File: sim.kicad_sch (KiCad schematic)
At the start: 40 parts

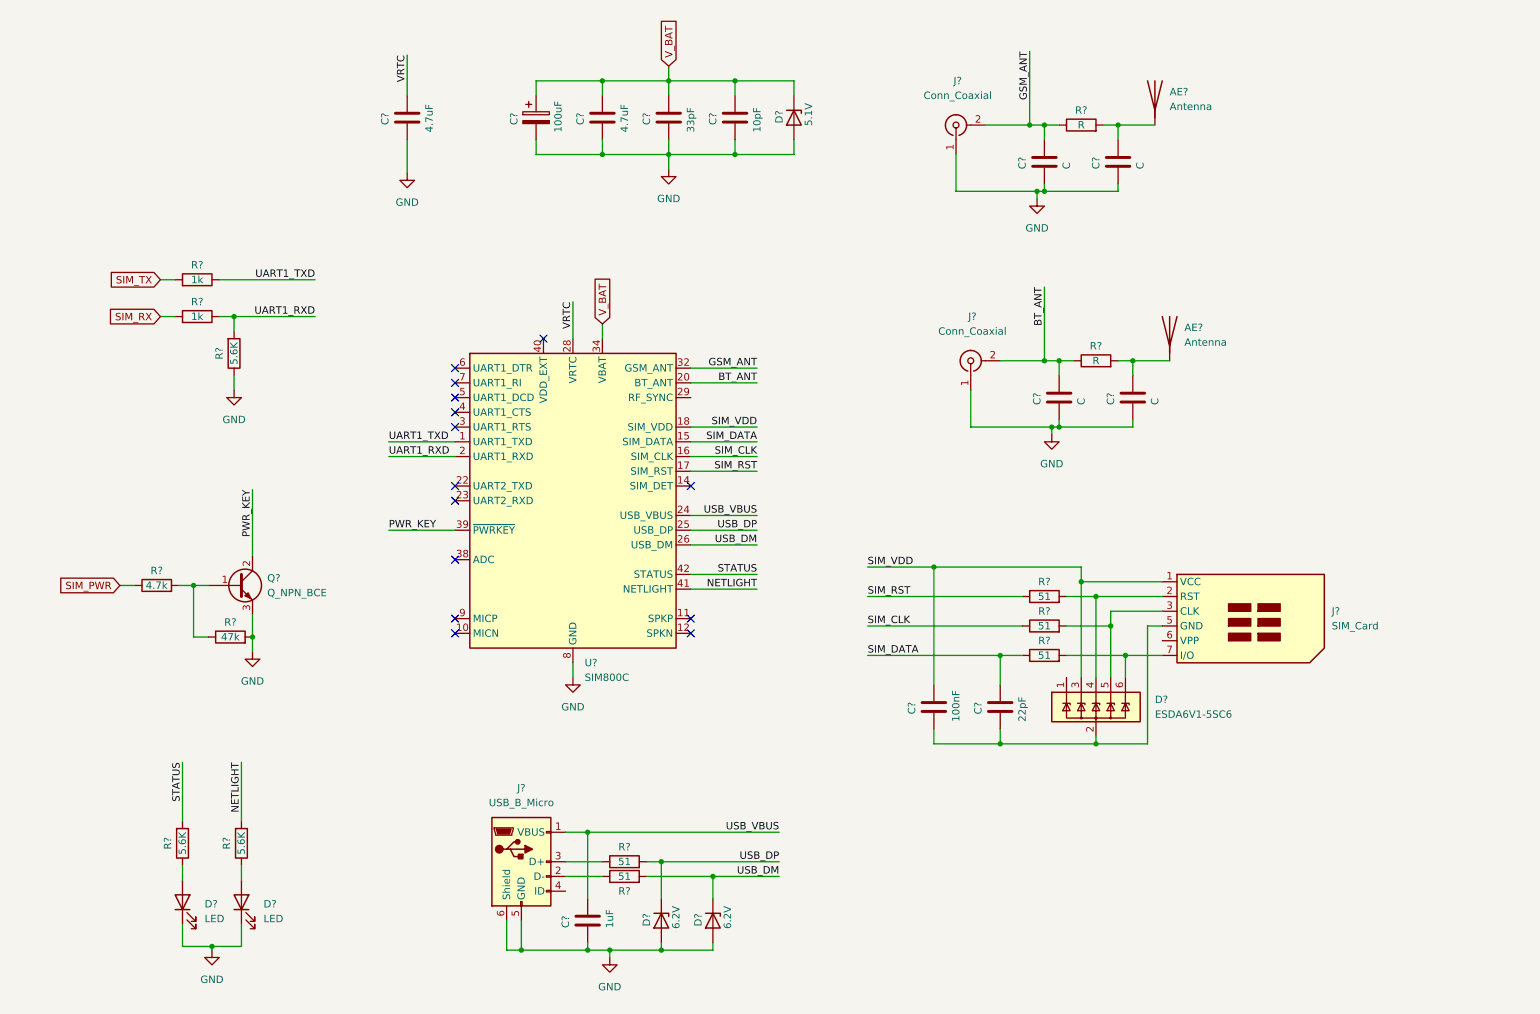
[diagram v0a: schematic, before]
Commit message: Create scheme for MCU with peripheries
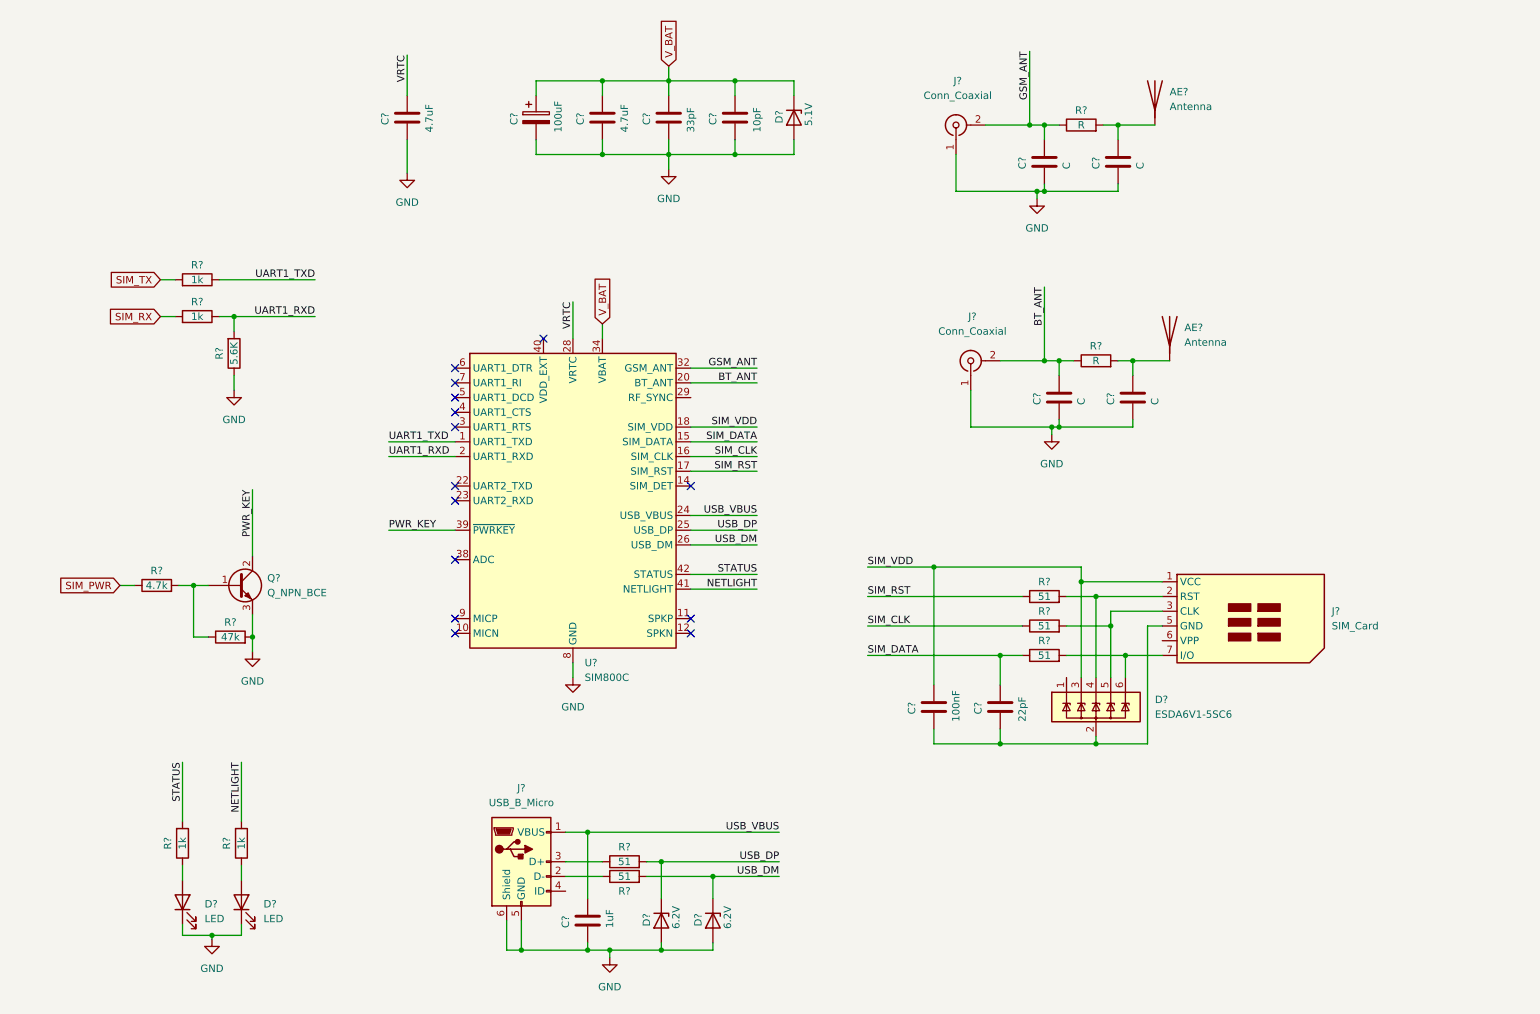
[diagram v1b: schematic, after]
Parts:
- R? (x2): value 5.6K -> 1k
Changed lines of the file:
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@@
   (junction (at 134.62 180.34) (diameter 0) (color 0 0 0 0)
   )
-  (junction (at 57.15 179.705) (diameter 0) (color 0 0 0 0)
+  (junction (at 57.15 177.8) (diameter 0) (color 0 0 0 0)
   )
   (junction (at 212.09 124.46) (diameter 0) (color 0 0 0 0)
@@
     (stroke (width 0) (type default) (color 0 0 0 0))
   )
-  (wire (pts (xy 57.15 179.705) (xy 52.07 179.705))
+  (wire (pts (xy 57.15 177.8) (xy 52.07 177.8))
     (stroke (width 0) (type default) (color 0 0 0 0))
   )
@@
     (stroke (width 0) (type default) (color 0 0 0 0))
   )
-  (wire (pts (xy 57.15 179.705) (xy 62.23 179.705))
+  (wire (pts (xy 57.15 177.8) (xy 62.23 177.8))
     (stroke (width 0) (type default) (color 0 0 0 0))
   )
@@
     (stroke (width 0) (type default) (color 0 0 0 0))
   )
-  (wire (pts (xy 52.07 175.895) (xy 52.07 179.705))
+  (wire (pts (xy 52.07 175.895) (xy 52.07 177.8))
     (stroke (width 0) (type default) (color 0 0 0 0))
   )
@@
     (stroke (width 0) (type default) (color 0 0 0 0))
   )
-  (wire (pts (xy 62.23 175.895) (xy 62.23 179.705))
+  (wire (pts (xy 62.23 175.895) (xy 62.23 177.8))
     (stroke (width 0) (type default) (color 0 0 0 0))
   )
@@
     (stroke (width 0) (type default) (color 0 0 0 0))
   )
-  (wire (pts (xy 57.15 180.34) (xy 57.15 179.705))
+  (wire (pts (xy 57.15 178.435) (xy 57.15 177.8))
     (stroke (width 0) (type default) (color 0 0 0 0))
   )
@@
     (in_bom yes) (on_board yes)
     (property "Reference" "R?" (id 0) (at 59.69 161.925 90))
-    (property "Value" "5.6K" (id 1) (at 62.23 161.925 90))
+    (property "Value" "1k" (id 1) (at 62.23 161.925 90))
     (property "Footprint" "" (id 2) (at 60.452 161.925 90)
       (effects (font (size 1.27 1.27)) hide)
@@
     (in_bom yes) (on_board yes)
     (property "Reference" "R?" (id 0) (at 49.53 161.925 90))
-    (property "Value" "5.6K" (id 1) (at 52.07 161.925 90))
+    (property "Value" "1k" (id 1) (at 52.07 161.925 90))
     (property "Footprint" "" (id 2) (at 50.292 161.925 90)
       (effects (font (size 1.27 1.27)) hide)
@@
     (pin "1")
   )
-  (symbol (lib_id "power:GND") (at 57.15 180.34 0) (unit 1)
-    (in_bom yes) (on_board yes) (fields_autoplaced)
-    (property "Reference" "#PWR?" (id 0) (at 57.15 186.69 0)
-      (effects (font (size 1.27 1.27)) hide)
-    )
-    (property "Value" "GND" (id 1) (at 57.15 185.42 0))
-    (property "Footprint" "" (id 2) (at 57.15 180.34 0)
-      (effects (font (size 1.27 1.27)) hide)
-    )
-    (property "Datasheet" "" (id 3) (at 57.15 180.34 0)
-      (effects (font (size 1.27 1.27)) hide)
-    )
+  (symbol (lib_id "power:GND") (at 57.15 178.435 0) (unit 1)
+    (in_bom yes) (on_board yes) (fields_autoplaced)
+    (property "Reference" "#PWR?" (id 0) (at 57.15 184.785 0)
+      (effects (font (size 1.27 1.27)) hide)
+    )
+    (property "Value" "GND" (id 1) (at 57.15 183.515 0))
+    (property "Footprint" "" (id 2) (at 57.15 178.435 0)
+      (effects (font (size 1.27 1.27)) hide)
+    )
+    (property "Datasheet" "" (id 3) (at 57.15 178.435 0)
+      (effects (font (size 1.27 1.27)) hide)
+    )

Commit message: Change layout
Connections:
- net NETLIGHT: no longer names the net of R?.2
- net NETLIGHT: now also U?.42 (STATUS); no longer U?.41 (NETLIGHT)
- net STATUS: no longer names the net of R?.2
- net STATUS: now also U?.41 (NETLIGHT); no longer U?.42 (STATUS)
- net UART1_RXD: no longer names the net of R?.1, R?.2, U?.2 (UART1_RXD)
- net UART1_TXD: no longer names the net of R?.1, U?.1 (UART1_TXD)
- net VRTC: no longer names the net of C?.1, U?.28 (VRTC)
- no-connect marks 14 -> 15
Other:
- moved on the sheet: AE?, C?, D?, J?, Q?, R?

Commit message: Add TSP62851x library and LDO on PSU scheme
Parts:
- removed AE? (x2): Antenna, symbol Device:Antenna
- removed C? (x4): C, symbol Device:C
- removed J?: Conn_Coaxial, symbol Connector:Conn_Coaxial
- removed R? (x2): R, symbol Device:R
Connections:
- net BT_ANT: no longer names the net of U?.20 (BT_ANT)
- net V_BAT renamed +4V0
- no-connect marks 15 -> 20
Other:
- moved on the sheet: J?

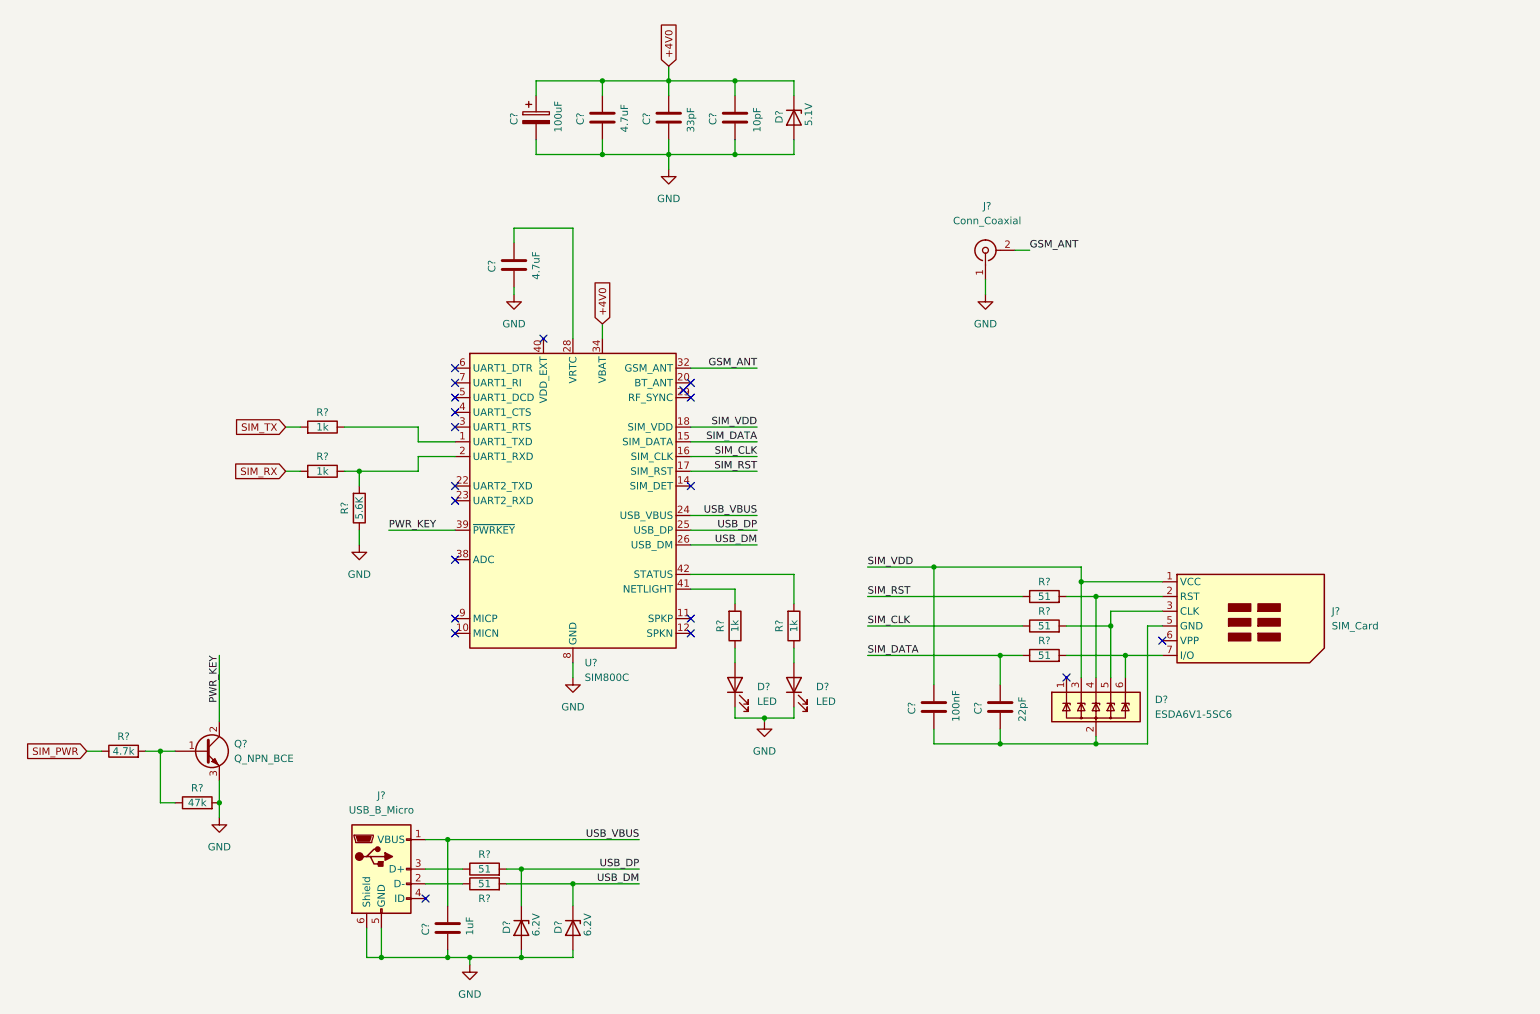
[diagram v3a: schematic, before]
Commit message: Complete schemes, run ERD check tool.
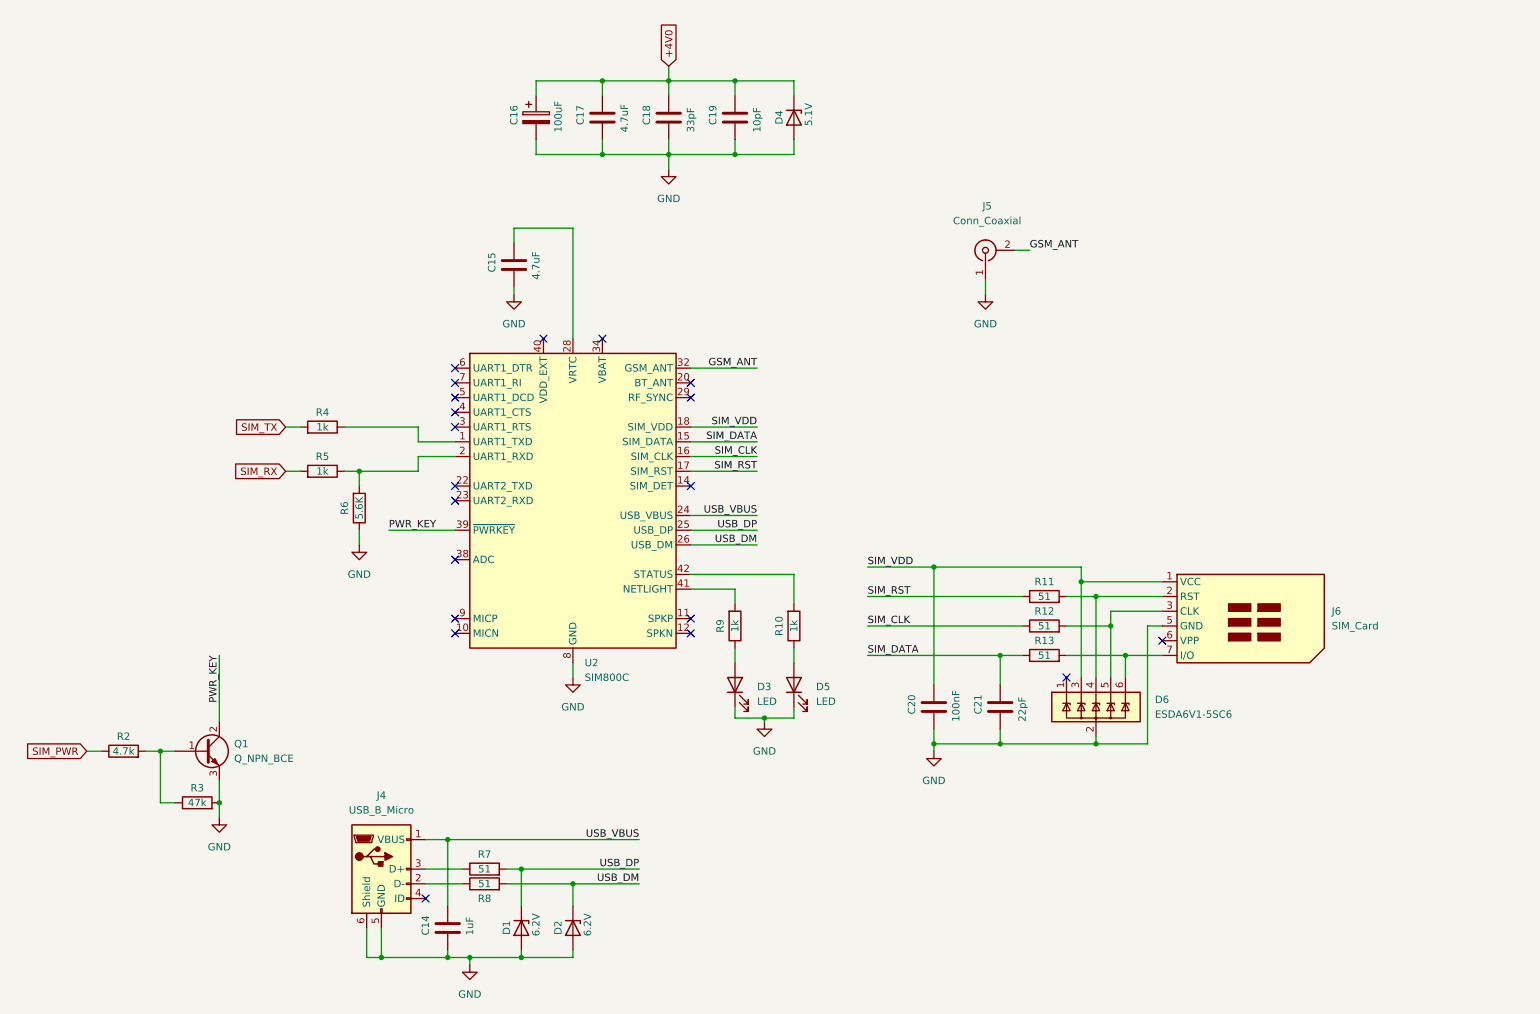
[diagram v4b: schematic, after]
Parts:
- gave numbers to parts that had none: 31
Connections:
- net +4V0: no longer U2.34 (VBAT), U2.35 (VBAT)
- net GND: now also C20.2, C21.2, D6.2 (GND), J6.5 (GND)
- new net: U2.34 (VBAT), U2.35 (VBAT)
